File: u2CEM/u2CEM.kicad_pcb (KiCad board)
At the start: 4 copper layers, 168 x 70 mm, 16 parts, among them J1 PCIE_x4_10018784-10211TLF, J2 PSAS4M2130021TR

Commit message: new version
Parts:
- J1: value PCIE_x4_10018784-10211TLF -> PCIE_x4_PCIE-064-02-S-D-RA; footprint PCIe:PCIe_x4_0018784-1228695 -> U2:SAMTEC_PCIE-064-02-X-D-EMS2-BG
- J2: footprint PCIe:PSAS4M2130021TR -> U2:PSAS4M2130021TR
- R1, R2, R3, R4: moved to B.Cu
- moved J2 285.2 mm to (102.0, 204.0), turned to 90 degrees
- moved R11 273.1 mm to (108.5, 214.8)
- moved R10 271.9 mm to (108.5, 209.5), turned to -90 degrees
- moved R6 146.8 mm to (109.0, 204.0), turned to 180 degrees
- moved R7 144.3 mm to (107.4, 202.2), turned to 180 degrees
- moved R5 143.0 mm to (109.0, 206.0), turned to 180 degrees
- moved R1 129.1 mm to (269.5, 225.5), turned to 90 degrees
- moved G*** 125.5 mm to (170.3, 177.2), turned to 0 degrees
- moved R3 121.8 mm to (267.0, 225.5)
- moved J1 121.0 mm to (260.8, 216.1), turned to 180 degrees
- moved R4 120.6 mm to (265.0, 225.5)
- moved R2 110.2 mm to (245.3, 223.3)
- moved D1 59.0 mm to (221.4, 193.7)
- moved R8 59.0 mm to (216.9, 193.7)
- moved D2 56.0 mm to (221.4, 186.2)
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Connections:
- J1 pad A21: /PER1_N -> /PER1_P
- J1 pad A22: /PER1_P -> /PER1_N
- J1 pad A25: /PER2_N -> /PER2_P
- J1 pad A26: /PER2_P -> /PER2_N
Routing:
- net Net-(J2-PadP4): track 167.5 -> 7.77 mm, vias 4 -> 0
- net Net-(J1-PadB17): track 38.9 -> 164.0 mm, vias 0 -> 3
- net GND: track 48.4 -> 157.0 mm, vias 639 -> 84
- net +12V: track 0.00 -> 60.3 mm, vias 0 -> 19
- net /PET0_P: track 163.6 -> 218.5 mm, vias 1 -> 3
- net /PET0_N: track 163.7 -> 216.6 mm, vias 1 -> 3
- net /PET1_P: track 150.4 -> 198.1 mm, vias 1 -> 3
- net /PET1_N: track 150.3 -> 196.3 mm, vias 1 -> 3
- net /PET2_P: track 142.5 -> 181.6 mm, vias 1 -> 3
- net /PET2_N: track 142.4 -> 179.7 mm, vias 1 -> 3
- net /REFCLK_P: track 175.4 -> 208.6 mm, vias 1 -> 2
- net /REFCLK_N: track 175.4 -> 206.7 mm, vias 1 -> 2
- net /PER0_P: track 164.4 -> 195.3 mm, vias 1 -> 2
- net /PER0_N: track 164.3 -> 194.7 mm, vias 1 -> 2
- net /PET3_P: track 136.1 -> 166.2 mm, vias 1 -> 3
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- added copper zone on In2.Cu, net +12V
- added copper zone on In3.Cu, net +3.3V
- added copper zone on In3.Cu, net GND
- added copper zone on In4.Cu, net GND
- removed copper zone on In2.Cu, net +3.3V
- removed copper zone on B.Cu, net GND
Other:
- board size 168 x 70 mm -> 188 x 66.8 mm
- copper layers 4 -> 6
- board text added: "Kludge.2r2"
- board text removed: "Kludge.2"

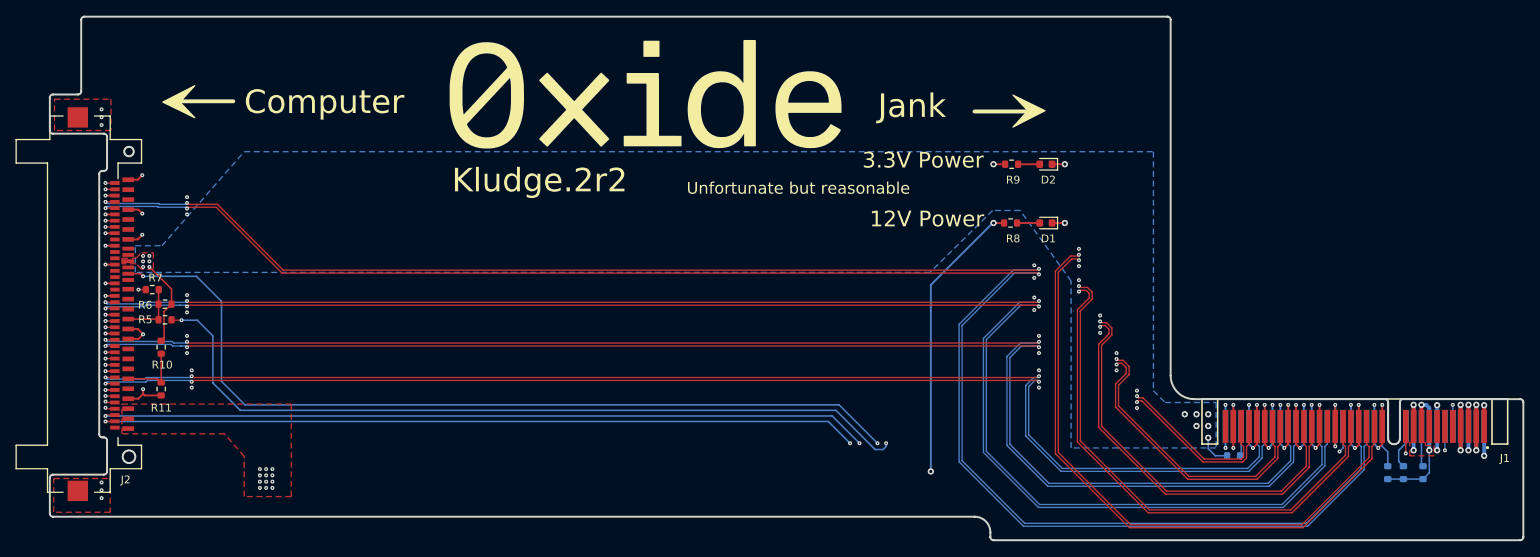
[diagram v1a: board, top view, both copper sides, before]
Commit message: fixed outline and DRCs
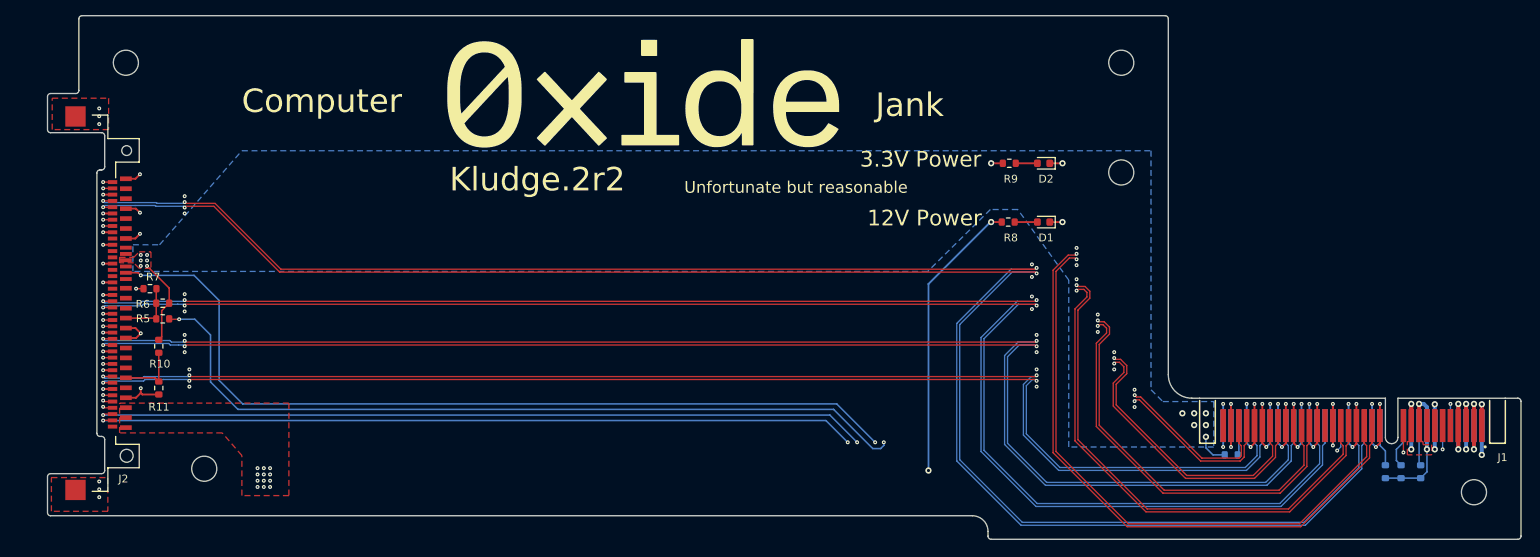
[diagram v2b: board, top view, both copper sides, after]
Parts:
- added REF**: MountingHole_3.2mm_M3, MountingHole:MountingHole_3.2mm_M3, F.Cu at (276.0, 228.0)
- added REF**: MountingHole_3.2mm_M3, MountingHole:MountingHole_3.2mm_M3, F.Cu at (114.0, 225.0)
- added REF**: MountingHole_3.2mm_M3, MountingHole:MountingHole_3.2mm_M3, F.Cu at (104.0, 173.2)
- added REF**: MountingHole_3.2mm_M3, MountingHole:MountingHole_3.2mm_M3, F.Cu at (231.0, 173.2)
- added REF**: MountingHole_3.2mm_M3, MountingHole:MountingHole_3.2mm_M3, F.Cu at (231.0, 187.2)
- moved G*** 0.32 mm to (170.0, 177.1)
- moved R1 0.32 mm to (269.2, 225.4)
- moved R3 0.32 mm to (266.7, 225.4)
- moved R4 0.32 mm to (264.7, 225.4)
- moved R8 0.32 mm to (216.6, 193.5)
- moved J2 0.32 mm to (101.7, 203.9)
- moved R10 0.32 mm to (108.2, 209.4)
- moved R5 0.32 mm to (108.7, 205.9)
- moved R6 0.32 mm to (108.7, 203.9)
- moved R7 0.32 mm to (107.1, 202.0)
- moved R11 0.32 mm to (108.2, 214.7)
- moved D1 0.32 mm to (221.1, 193.5)
- moved D2 0.32 mm to (221.1, 186.0)
- moved R9 0.32 mm to (216.7, 186.0)
- moved R2 0.32 mm to (245.0, 223.2)
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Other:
- outline, holes or cut-outs redrawn

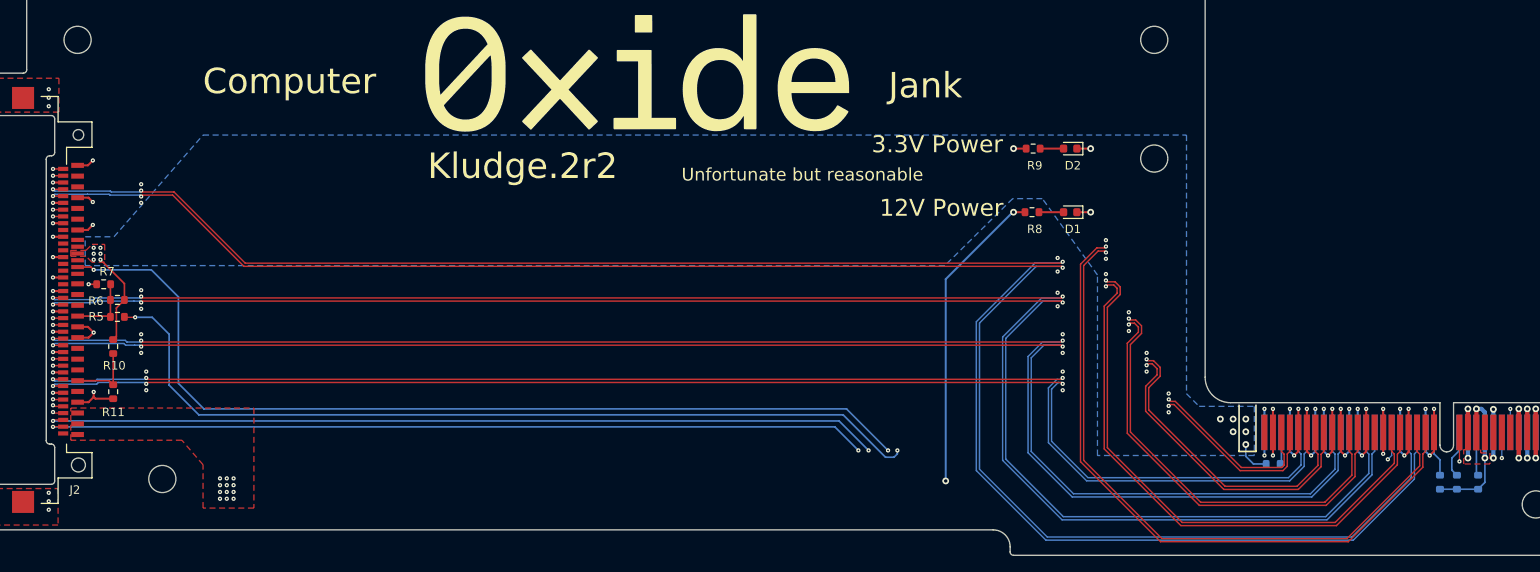
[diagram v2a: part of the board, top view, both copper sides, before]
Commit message: Package sent to tapeout
final PCB package with updated trace width/spacing based on Ian calculating the required dimensions correctly instead of doing it wrong like I did.

MCAD design still in flux
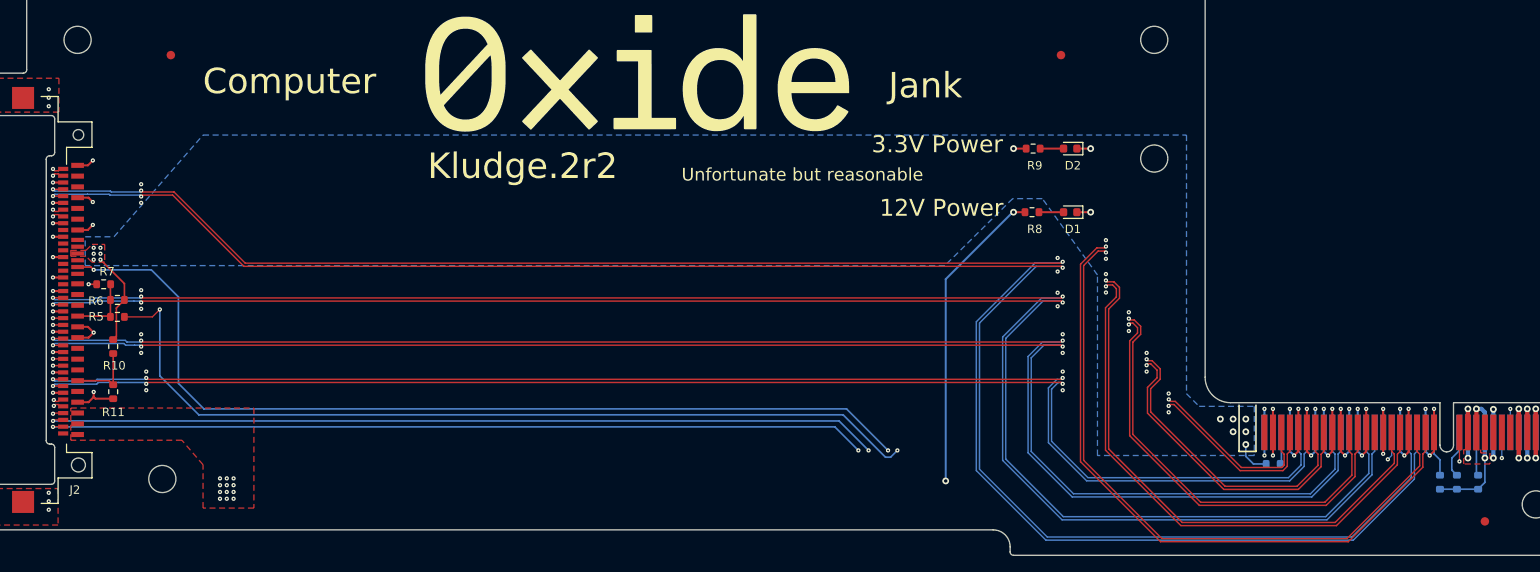
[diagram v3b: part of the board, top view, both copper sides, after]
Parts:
- added REF**: Fiducial_1mm_Mask3mm, Fiducial:Fiducial_1mm_Mask3mm, F.Cu at (115.0, 175.0)
- added REF**: Fiducial_1mm_Mask3mm, Fiducial:Fiducial_1mm_Mask3mm, F.Cu at (270.0, 230.0)
- added REF**: Fiducial_1mm_Mask3mm, Fiducial:Fiducial_1mm_Mask3mm, F.Cu at (220.0, 175.0)
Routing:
- net Net-(J1-PadB17): track 164.0 -> 165.6 mm
- net /PER1_P: track 180.9 -> 179.5 mm
- net /PER1_N: track 180.2 -> 178.9 mm
- net /PER3_N: track 153.9 -> 154.5 mm
- net GND: vias 84 -> 85
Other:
- board text added: "Without length-matching, diff pairs within 2mm for phase mismatch, which is about 6.7% of a UI at 5Gbps."
